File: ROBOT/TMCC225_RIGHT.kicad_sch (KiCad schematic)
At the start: 16 parts, among them J4 Conn_01x04, U1 TMC2225-SA-T

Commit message: Schema OK
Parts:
- C11, C14: footprint Capacitor_SMD:C_0603_1608Metric_Pad1.08x0.95mm_HandSolder -> Capacitor_SMD:C_0805_2012Metric_Pad1.18x1.45mm_HandSolder
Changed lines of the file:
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@@
 			)
 		)
-		(property "Footprint" "Capacitor_SMD:C_0603_1608Metric_Pad1.08x0.95mm_HandSolder"
+		(property "Footprint" "Capacitor_SMD:C_0805_2012Metric_Pad1.18x1.45mm_HandSolder"
 			(at 161.29 58.7248 0)
 			(effects
@@
 			)
 		)
-		(property "Footprint" "Capacitor_SMD:C_0603_1608Metric_Pad1.08x0.95mm_HandSolder"
+		(property "Footprint" "Capacitor_SMD:C_0805_2012Metric_Pad1.18x1.45mm_HandSolder"
 			(at 161.29 49.8348 0)
 			(effects

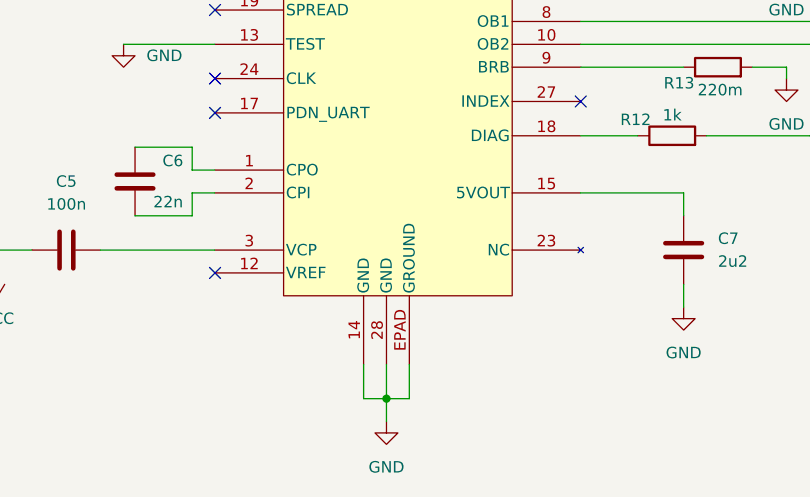
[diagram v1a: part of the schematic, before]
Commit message: GND PAD 29 TMC22225
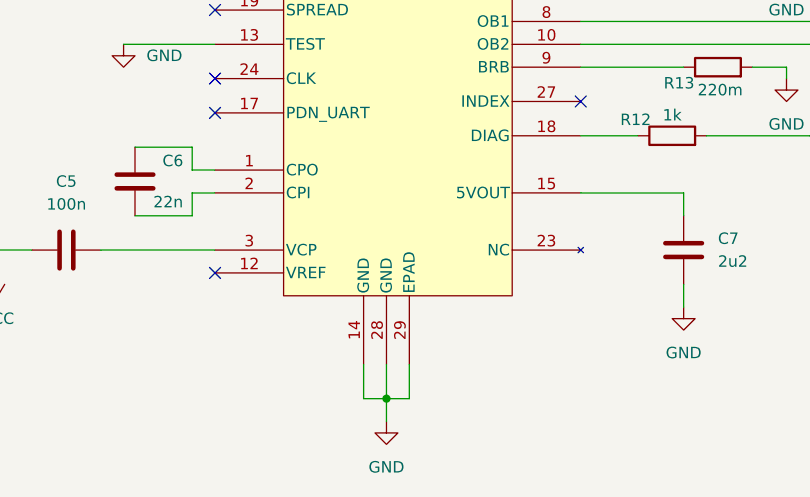
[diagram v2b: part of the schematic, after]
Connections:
- net GND: now also U1.29 (EPAD); no longer U1.EPAD (GROUND)
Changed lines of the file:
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@@
 		(pin "2"
 		)
-		(pin "EPAD"
+		(pin "29"
 		)
 		(pin "14"

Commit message: add condo
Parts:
- added C10: 10uF, Capacitor_SMD:C_0805_2012Metric_Pad1.18x1.45mm_HandSolder, symbol Device:C
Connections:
- net GND: now also C10.2
- net VCC: now also C10.1
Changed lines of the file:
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@@
+	)
+	(junction
+		(at 149.86 40.64)
+		(diameter 0)
+		(color 0 0 0 0)
 	)
 	(junction
@@
 	(wire
 		(pts
+			(xy 149.86 40.64) (xy 153.67 40.64)
+		)
+		(stroke
+			(width 0)
+			(type default)
+		)
+	)
+	(wire
+		(pts
 			(xy 133.35 66.04) (xy 133.35 68.58)
 		)
@@
 	(wire
 		(pts
-			(xy 149.86 38.1) (xy 149.86 50.8)
+			(xy 149.86 38.1) (xy 149.86 40.64)
 		)
 		(stroke
@@
 	(wire
 		(pts
+			(xy 163.83 40.64) (xy 163.83 43.18)
+		)
+		(stroke
+			(width 0)
+			(type default)
+		)
+	)
+	(wire
+		(pts
 			(xy 149.86 59.69) (xy 153.67 59.69)
 		)
@@
 	(wire
 		(pts
+			(xy 149.86 40.64) (xy 149.86 50.8)
+		)
+		(stroke
+			(width 0)
+			(type default)
+		)
+	)
+	(wire
+		(pts
 			(xy 107.95 121.92) (xy 104.14 121.92)
 		)
@@
 		(pts
 			(xy 161.29 50.8) (xy 163.83 50.8)
+		)
+		(stroke
+			(width 0)
+			(type default)
+		)
+	)
+	(wire
+		(pts
+			(xy 161.29 40.64) (xy 163.83 40.64)
 		)
 		(stroke
@@
 	)
 	(symbol
+		(lib_id "Device:C")
+		(at 157.48 40.64 90)
+		(unit 1)
+		(exclude_from_sim no)
+		(in_bom yes)
+		(on_board yes)
+		(dnp no)
+		(property "Reference" "C10"
+			(at 157.734 35.052 90)
+			(effects
+				(font
+					(size 1.27 1.27)
+				)
+			)
+		)
+		(property "Value" "10uF"
+			(at 157.48 37.338 90)
+			(effects
+				(font
+					(size 1.27 1.27)
+				)
+			)
+		)
+		(property "Footprint" "Capacitor_SMD:C_0805_2012Metric_Pad1.18x1.45mm_HandSolder"
+			(at 161.29 39.6748 0)
+			(effects
+				(font
+					(size 1.27 1.27)
+				)
+				(hide yes)
+			)
+		)
+		(property "Datasheet" "~"
+			(at 157.48 40.64 0)
+			(effects
+				(font
+					(size 1.27 1.27)
+				)
+				(hide yes)
+			)
+		)
+		(property "Description" "Unpolarized capacitor"
+			(at 157.48 40.64 0)
+			(effects
+				(font
+					(size 1.27 1.27)
+				)
+				(hide yes)
+			)
+		)
+		(pin "1"
+		)
+		(pin "2"
+		)
+		(instances
+			(project "Robot"
+				(path "/f1dd5862-79ad-43be-9f5c-46baed2cd441/dd72f74b-5e7d-4592-90a6-8866feca75fb"
+					(reference "C10")
+					(unit 1)
+				)
+			)
+		)
+	)
+	(symbol
 		(lib_id "Connector_Generic:Conn_01x04")
 		(at 213.36 88.9 0)
@@
 					(unit 1)
 				)
+			)
+		)
+	)
+	(symbol
+		(lib_id "power:GND")
+		(at 163.83 43.18 0)
+		(unit 1)
+		(exclude_from_sim no)
+		(in_bom yes)
+		(on_board yes)
+		(dnp no)
+		(fields_autoplaced yes)
+		(property "Reference" "#PWR035"
+			(at 163.83 49.53 0)
+			(effects
+				(font
+					(size 1.27 1.27)
+				)
+				(hide yes)
+			)
+		)
+		(property "Value" "GND"
+			(at 163.83 48.26 0)
+			(effects
+				(font
+					(size 1.27 1.27)
+				)
+			)
+		)
+		(property "Footprint" ""
+			(at 163.83 43.18 0)
+			(effects
+				(font
+					(size 1.27 1.27)
+				)
+				(hide yes)
+			)
+		)
+		(property "Datasheet" ""
+			(at 163.83 43.18 0)
+			(effects
+				(font
+					(size 1.27 1.27)
+				)
+				(hide yes)
+			)
+		)
+		(property "Description" "Power symbol creates a global label with name \"GND\" , ground"
+			(at 163.83 43.18 0)
+			(effects
+				(font
+					(size 1.27 1.27)
+				)
+				(hide yes)
+			)
+		)
+		(pin "1"
+		)
+		(instances
+			(project "Robot"
+				(path "/f1dd5862-79ad-43be-9f5c-46baed2cd441/dd72f74b-5e7d-4592-90a6-8866feca75fb"
+					(reference "#PWR035")
+					(unit 1)
+				)

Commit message: update PCB
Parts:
- C11, C14: footprint Capacitor_SMD:C_0805_2012Metric_Pad1.18x1.45mm_HandSolder -> Capacitor_SMD:C_0603_1608Metric_Pad1.08x0.95mm_HandSolder
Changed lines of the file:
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@@
 			)
 		)
-		(property "Footprint" "Capacitor_SMD:C_0805_2012Metric_Pad1.18x1.45mm_HandSolder"
+		(property "Footprint" "Capacitor_SMD:C_0603_1608Metric_Pad1.08x0.95mm_HandSolder"
 			(at 161.29 58.7248 0)
 			(effects
@@
 			)
 		)
-		(property "Footprint" "Capacitor_SMD:C_0805_2012Metric_Pad1.18x1.45mm_HandSolder"
+		(property "Footprint" "Capacitor_SMD:C_0603_1608Metric_Pad1.08x0.95mm_HandSolder"
 			(at 161.29 49.8348 0)
 			(effects
